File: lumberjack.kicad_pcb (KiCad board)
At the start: 2 copper layers, 285.4 x 94.9 mm, 150 parts, among them J1 USB_OTG, J2 AVR_ISP_6, SW1 RESET, SW2 BOOT, U1 ATMEGA328-PU, Y1 16MHz

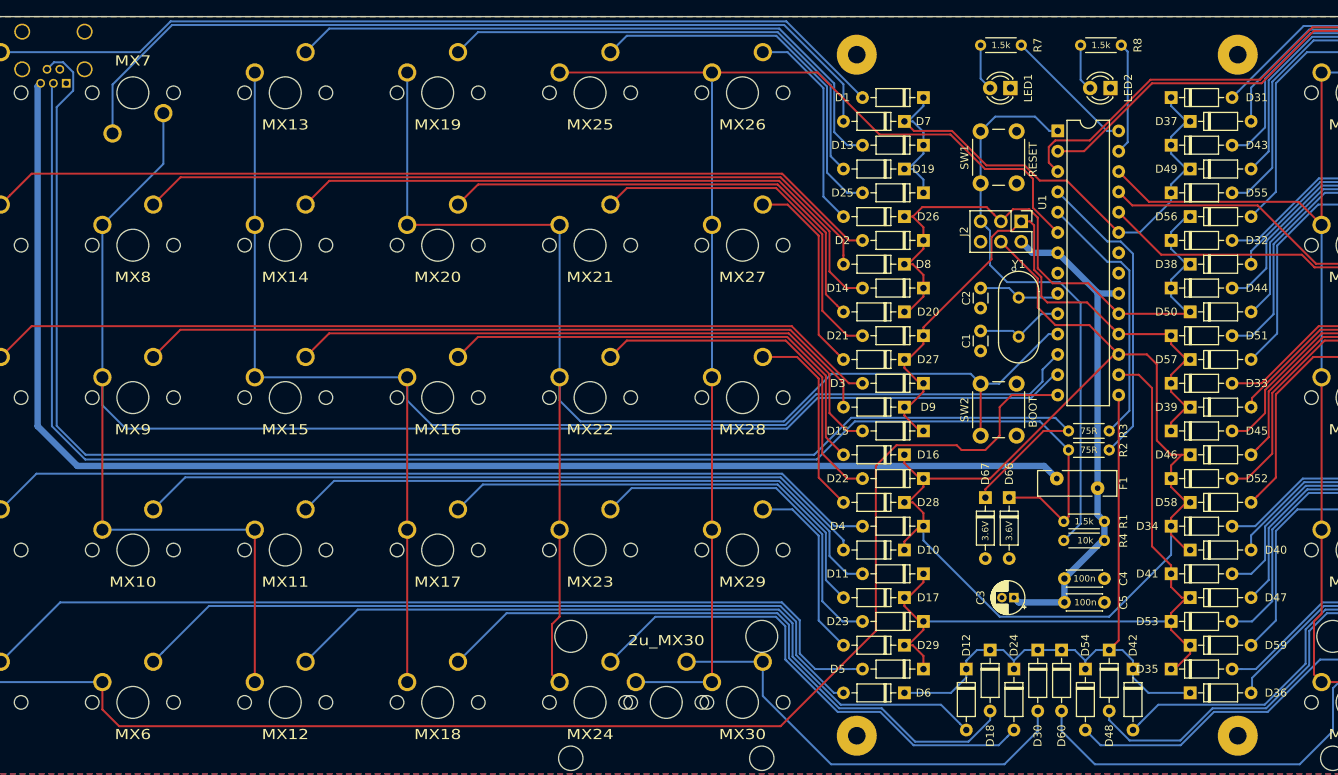
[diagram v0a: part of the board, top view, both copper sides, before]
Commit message: Add center post mounting hole
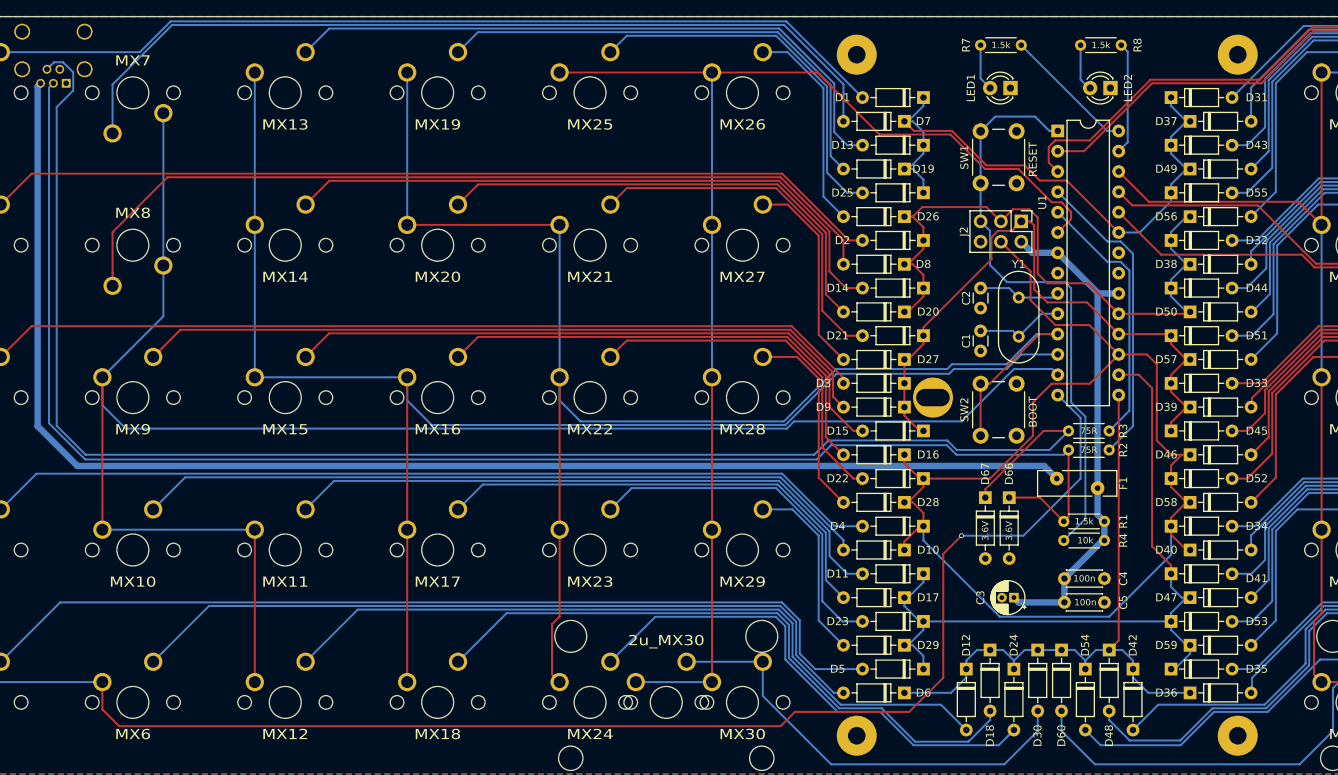
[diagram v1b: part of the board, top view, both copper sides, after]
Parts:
- added H5: M2, MountingHole:MountingHole_2.2mm_M2, F.Cu at (138.1, 102.4)
- moved D3 2.38 mm to (134.5, 100.6)
- turned MX8 to 180 degrees
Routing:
- net Net-(D8-Pad2): track 94.0 -> 107.2 mm
- net /COL3: track 174.3 -> 185.5 mm
- net /COL0: track 254.9 -> 259.5 mm, vias 0 -> 1
- net /ROW2: track 82.6 -> 80.1 mm
- net /ROW3: track 149.7 -> 152.2 mm
- net /COL4: track 158.4 -> 160.1 mm
- net Net-(D3-Pad2): track 112.3 -> 110.6 mm
- net Net-(D66-Pad1): track 192.4 -> 190.8 mm
- net /RESET: track 72.2 -> 73.1 mm
- net /COL2: track 185.3 -> 184.4 mm
- net /COL1: track 220.2 -> 220.8 mm
- net GND: vias 1 -> 0
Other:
- board text added: "POST"

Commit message: Move components to allow fuse to lie flat
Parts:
- removed the H5 at (138.1, 102.4)
- added H7: M2, lumberjack:MountingSlot_M2, F.Cu at (138.1, 102.4)
- moved R4 13.7 mm to (160.7, 106.6)
- moved D67 12.2 mm to (154.9, 121.4), turned to 0 degrees
- moved F1 12.0 mm to (141.7, 113.7), turned to 270 degrees
- moved D66 8.09 mm to (154.9, 118.5), turned to 0 degrees
- moved D36 6.33 mm to (166.1, 134.5), turned to 270 degrees
- moved D6 6.33 mm to (138.7, 134.5), turned to 270 degrees
- moved J2 5.61 mm to (144.1, 82.7), turned to 90 degrees
- moved R1 4.33 mm to (155.7, 113.7)
- moved R2 2.45 mm to (160.7, 111.3)
- moved R3 2.45 mm to (160.7, 108.9)
- moved C4 2.15 mm to (155.7, 126.8)
- moved C5 2.15 mm to (155.7, 129.8)
- moved D35 1.33 mm to (169.1, 136.9), turned to 270 degrees
- moved C3 1.33 mm to (147.0, 128.0)
- moved D5 1.33 mm to (135.7, 136.9), turned to 270 degrees
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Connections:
- J2 pad 1: /ROW2 -> GND
- J2 pad 2: +5V -> /RESET
- J2 pad 3: /ROW1 -> /ROW3
- J2 pad 4: /ROW3 -> /ROW1
- J2 pad 5: /RESET -> +5V
- J2 pad 6: GND -> /ROW2
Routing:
- net +5V: track 62.7 -> 81.7 mm
- net Net-(D6-Pad2): track 96.1 -> 115.1 mm
- net Net-(D36-Pad2): track 99.8 -> 115.9 mm
- net /ROW3: track 152.2 -> 165.0 mm
- net Net-(D5-Pad2): track 116.7 -> 128.4 mm
- net Net-(F1-Pad1): track 173.1 -> 161.7 mm
- net /RESET: track 73.1 -> 62.1 mm
- net Net-(D35-Pad2): track 119.3 -> 129.2 mm
- net Net-(D66-Pad1): track 190.8 -> 182.1 mm
- net /ROW5: track 79.3 -> 73.6 mm
- net Net-(D18-Pad2): track 80.4 -> 86.0 mm
- net Net-(D24-Pad2): track 62.7 -> 67.5 mm
- net Net-(D48-Pad2): track 84.8 -> 89.2 mm
- net Net-(D54-Pad2): track 61.7 -> 66.1 mm
- net /USB_D+: track 38.4 -> 41.8 mm
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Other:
- board text added: "GND"
- board text added: "ISP"
- board text added: "MISO"
- board text added: "MOSI"
- board text added: "RESET"
- board text added: "SCLK"
- board text added: "VCC"

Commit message: Update gerbers
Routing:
- net Net-(D54-Pad2): track 66.1 -> 69.2 mm
- net Net-(D48-Pad2): track 89.2 -> 86.9 mm
- net Net-(D36-Pad2): track 115.9 -> 116.4 mm
- net GND: vias 0 -> 3

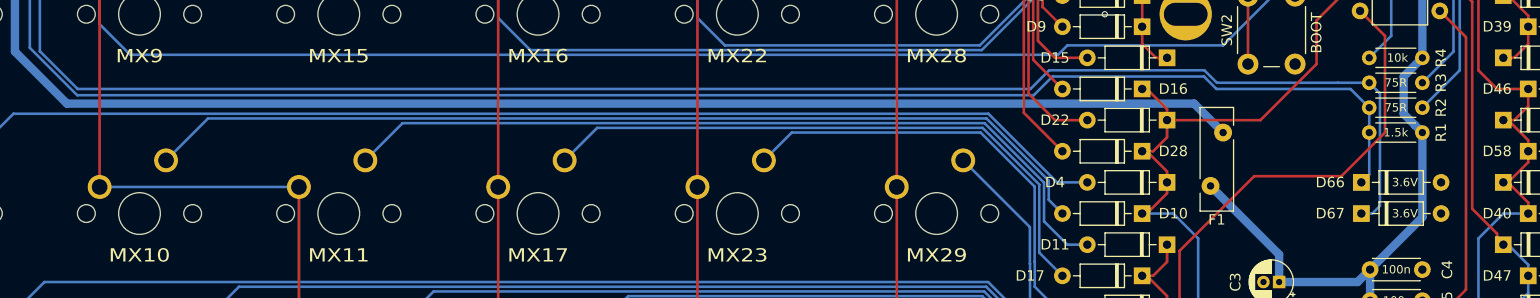
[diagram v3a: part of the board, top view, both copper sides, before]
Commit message: Adjust fuse footprint
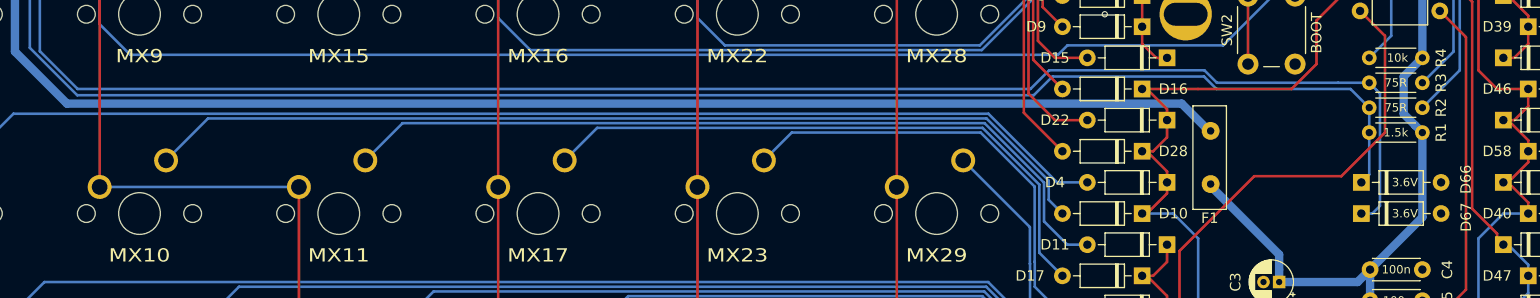
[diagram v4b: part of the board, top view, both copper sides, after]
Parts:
- moved F1 2.66 mm to (140.5, 116.1)
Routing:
- net Net-(F1-Pad1): track 161.7 -> 160.5 mm
- net /ROW3: track 165.0 -> 166.2 mm
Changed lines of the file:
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@@
     (thickness 1.6)
     (drawings 140)
-    (tracks 815)
+    (tracks 817)
     (zones 0)
     (modules 151)
@@
     (uvia_drill 0.1)
   )
+  (module Fuse:Fuse_Bourns_MF-RHT100 (layer F.Cu)
+    (at 140.493868 116.086035 270)
+    (descr "PTC Resettable Fuse, Ihold = 1.0A, Itrip=1.8A, http://www.bourns.com/docs/product-datasheets/mfrht.pdf")
+    (tags "ptc resettable fuse polyfuse THT")
+    (fp_text reference F1 (at 5.794382 0.087313) (layer F.SilkS)
+      (effects (font (size 1 1) (thickness 0.15)))
+    )
+    (fp_text value 100mA (at 0.01 2.592 270) (layer F.Fab)
+      (effects (font (size 1 1) (thickness 0.15)))
+    )
+    (fp_line (start -4.84 -1.408) (end -4.84 1.592) (layer F.Fab) (width 0.1))
+    (fp_line (start -4.84 1.592) (end 4.86 1.592) (layer F.Fab) (width 0.1))
+    (fp_line (start 4.86 1.592) (end 4.86 -1.408) (layer F.Fab) (width 0.1))
+    (fp_line (start 4.86 -1.408) (end -4.84 -1.408) (layer F.Fab) (width 0.1))
+    (fp_line (start -4.94 -1.508) (end 4.96 -1.508) (layer F.SilkS) (width 0.12))
+    (fp_line (start -4.94 1.692) (end 4.94 1.692) (layer F.SilkS) (width 0.12))
+    (fp_line (start -4.94 -1.508) (end -4.94 1.692) (layer F.SilkS) (width 0.12))
+    (fp_line (start 4.96 -1.508) (end 4.96 1.692) (layer F.SilkS) (width 0.12))
+    (fp_line (start -5.09 -1.658) (end -5.09 1.842) (layer F.CrtYd) (width 0.05))
+    (fp_line (start -5.09 1.842) (end 5.11 1.842) (layer F.CrtYd) (width 0.05))
+    (fp_line (start 5.11 1.842) (end 5.11 -1.658) (layer F.CrtYd) (width 0.05))
+    (fp_line (start 5.11 -1.658) (end -5.09 -1.658) (layer F.CrtYd) (width 0.05))
+    (fp_text user %R (at 0.01 0.092 270) (layer F.Fab)
+      (effects (font (size 1 1) (thickness 0.15)))
+    )
+    (pad 1 thru_hole circle (at -2.54 0 270) (size 1.71 1.71) (drill 0.71) (layers *.Cu *.Mask)
+      (net 26 "Net-(F1-Pad1)"))
+    (pad 2 thru_hole circle (at 2.54 0 270) (size 1.71 1.71) (drill 0.71) (layers *.Cu *.Mask)
+      (net 1 +5V))
+    (model ${KISYS3DMOD}/Fuse.3dshapes/Fuse_Bourns_MF-RHT100.wrl
+      (at (xyz 0 0 0))
+      (scale (xyz 1 1 1))
+      (rotate (xyz 0 0 0))
+    )
+  )
   (module Diode_THT:D_DO-35_SOD27_P7.62mm_Horizontal (layer F.Cu)
     (at 141.684494 136.92199 270)
@@
     )
   )
-  (module Fuse:Fuse_Bourns_MF-RHT100 (layer F.Cu)
-    (at 141.684494 113.704783 270)
-    (descr "PTC Resettable Fuse, Ihold = 1.0A, Itrip=1.8A, http://www.bourns.com/docs/product-datasheets/mfrht.pdf")
-    (tags "ptc resettable fuse polyfuse THT")
-    (fp_text reference F1 (at 8.334382 0.595313) (layer F.SilkS)
-      (effects (font (size 1 1) (thickness 0.15)))
-    )
-    (fp_text value 100mA (at 2.55 3.1 90) (layer F.Fab)
-      (effects (font (size 1 1) (thickness 0.15)))
-    )
-    (fp_line (start -2.3 -0.9) (end -2.3 2.1) (layer F.Fab) (width 0.1))
-    (fp_line (start -2.3 2.1) (end 7.4 2.1) (layer F.Fab) (width 0.1))
-    (fp_line (start 7.4 2.1) (end 7.4 -0.9) (layer F.Fab) (width 0.1))
-    (fp_line (start 7.4 -0.9) (end -2.3 -0.9) (layer F.Fab) (width 0.1))
-    (fp_line (start -2.4 -1) (end -0.689 -1) (layer F.SilkS) (width 0.12))
-    (fp_line (start 0.689 -1) (end 7.5 -1) (layer F.SilkS) (width 0.12))
-    (fp_line (start -2.4 2.2) (end 4.412 2.2) (layer F.SilkS) (width 0.12))
-    (fp_line (start 5.789 2.2) (end 7.5 2.2) (layer F.SilkS) (width 0.12))
-    (fp_line (start -2.4 -1) (end -2.4 2.2) (layer F.SilkS) (width 0.12))
-    (fp_line (start 7.5 -1) (end 7.5 2.2) (layer F.SilkS) (width 0.12))
-    (fp_line (start -2.55 -1.15) (end -2.55 2.35) (layer F.CrtYd) (width 0.05))
-    (fp_line (start -2.55 2.35) (end 7.65 2.35) (layer F.CrtYd) (width 0.05))
-    (fp_line (start 7.65 2.35) (end 7.65 -1.15) (layer F.CrtYd) (width 0.05))
-    (fp_line (start 7.65 -1.15) (end -2.55 -1.15) (layer F.CrtYd) (width 0.05))
-    (fp_text user %R (at 2.55 0.6 90) (layer F.Fab)
-      (effects (font (size 1 1) (thickness 0.15)))
-    )
-    (pad 1 thru_hole circle (at 0 0 270) (size 1.71 1.71) (drill 0.71) (layers *.Cu *.Mask)
-      (net 26 "Net-(F1-Pad1)"))
-    (pad 2 thru_hole circle (at 5.1 1.2 270) (size 1.71 1.71) (drill 0.71) (layers *.Cu *.Mask)
-      (net 1 +5V))
-    (model ${KISYS3DMOD}/Fuse.3dshapes/Fuse_Bourns_MF-RHT100.wrl
-      (at (xyz 0 0 0))
-      (scale (xyz 1 1 1))
-      (rotate (xyz 0 0 0))
-    )
-  )
   (module lumberjack:USB_Mini-B (layer B.Cu)
     (at 29.76565 63.103178 180)
@@
     (descr "Diode, DO-35_SOD27 series, Axial, Horizontal, pin pitch=7.62mm, , length*diameter=4*2mm^2, , http://www.diodes.com/_files/packages/DO-35.pdf")
     (tags "Diode DO-35_SOD27 series Axial Horizontal pin pitch 7.62mm  length 4mm diameter 2mm")
-    (fp_text reference D66 (at -2.976565 0) (layer F.SilkS)
+    (fp_text reference D66 (at 9.989886 -0.291227 90) (layer F.SilkS)
       (effects (font (size 1 1) (thickness 0.15)))
     )
@@
     (descr "Diode, DO-35_SOD27 series, Axial, Horizontal, pin pitch=7.62mm, , length*diameter=4*2mm^2, , http://www.diodes.com/_files/packages/DO-35.pdf")
     (tags "Diode DO-35_SOD27 series Axial Horizontal pin pitch 7.62mm  length 4mm diameter 2mm")
-    (fp_text reference D67 (at -2.976565 0) (layer F.SilkS)
+    (fp_text reference D67 (at 10.012617 0.34656 90) (layer F.SilkS)
       (effects (font (size 1 1) (thickness 0.15)))
     )
@@
   (segment (start 164.86199 96.996308) (end 166.092327 98.226645) (width 0.25) (layer F.Cu) (net 6))
   (segment (start 161.329823 96.996308) (end 164.86199 96.996308) (width 0.25) (layer F.Cu) (net 6))
-  (segment (start 145.256372 112.514157) (end 136.326677 112.514157) (width 0.25) (layer F.Cu) (net 6) (status 20))
-  (segment (start 161.329823 97.036019) (end 157.704533 100.661309) (width 0.25) (layer F.Cu) (net 6))
-  (segment (start 150.614189 107.15634) (end 145.256372 112.514157) (width 0.25) (layer F.Cu) (net 6))
-  (segment (start 150.614189 102.98915) (end 150.614189 107.15634) (width 0.25) (layer F.Cu) (net 6))
-  (segment (start 152.94203 100.661309) (end 150.614189 102.98915) (width 0.25) (layer F.Cu) (net 6))
-  (segment (start 161.329823 96.996308) (end 161.329823 97.036019) (width 0.25) (layer F.Cu) (net 6))
-  (segment (start 157.704533 100.661309) (end 152.94203 100.661309) (width 0.25) (layer F.Cu) (net 6))
   (segment (start 150.30948 86.452241) (end 146.605746 82.748507) (width 0.25) (layer F.Cu) (net 6) (status 20))
   (segment (start 150.30948 90.223965) (end 150.30948 86.452241) (width 0.25) (layer F.Cu) (net 6))
@@
   (segment (start 170.854831 120.393852) (end 168.928266 118.467287) (width 0.25) (layer F.Cu) (net 6) (status 20))
   (segment (start 170.854831 121.443852) (end 170.854831 120.393852) (width 0.25) (layer F.Cu) (net 6) (status 10))
+  (segment (start 150.614189 107.15634) (end 148.232937 109.537592) (width 0.25) (layer F.Cu) (net 6))
+  (segment (start 152.94203 100.661309) (end 150.614189 102.98915) (width 0.25) (layer F.Cu) (net 6))
+  (segment (start 157.704533 100.661309) (end 152.94203 100.661309) (width 0.25) (layer F.Cu) (net 6))
+  (segment (start 161.329823 97.036019) (end 157.704533 100.661309) (width 0.25) (layer F.Cu) (net 6))
+  (segment (start 148.232937 109.537592) (end 139.303242 109.537592) (width 0.25) (layer F.Cu) (net 6))
+  (segment (start 150.614189 102.98915) (end 150.614189 107.15634) (width 0.25) (layer F.Cu) (net 6))
+  (segment (start 161.329823 96.996308) (end 161.329823 97.036019) (width 0.25) (layer F.Cu) (net 6))
+  (segment (start 139.303242 109.537592) (end 133.945425 109.537592) (width 0.25) (layer F.Cu) (net 6))
   (segment (start 165.497014 101.20321) (end 165.497014 120.989165) (width 0.25) (layer F.Cu) (net 7))
   (segment (start 167.878266 123.370417) (end 167.878266 124.420417) (width 0.25) (layer F.Cu) (net 7) (status 20))
@@
   (segment (start 154.265425 89.892263) (end 154.78138 89.376308) (width 0.25) (layer B.Cu) (net 25) (status 30))
   (segment (start 148.82825 89.892263) (end 154.265425 89.892263) (width 0.25) (layer B.Cu) (net 25) (status 30))
-  (segment (start 138.917304 110.937593) (end 141.684494 113.704783) (width 0.8) (layer B.Cu) (net 26))
+  (segment (start 140.33512 113.546035) (end 140.493868 113.546035) (width 0.8) (layer B.Cu) (net 26))
+  (segment (start 31.165651 110.937593) (end 137.726678 110.937593) (width 0.8) (layer B.Cu) (net 26))
+  (segment (start 137.726678 110.937593) (end 140.33512 113.546035) (width 0.8) (layer B.Cu) (net 26))
   (segment (start 26.193772 105.965714) (end 31.165651 110.937593) (width 0.8) (layer B.Cu) (net 26))
-  (segment (start 31.165651 110.937593) (end 138.917304 110.937593) (width 0.8) (layer B.Cu) (net 26))
   (segment (start 26.193772 63.475056) (end 26.193772 105.965714) (width 0.8) (layer B.Cu) (net 26))
   (segment (start 26.56565 63.103178) (end 26.193772 63.475056) (width 0.8) (layer B.Cu) (net 26))
